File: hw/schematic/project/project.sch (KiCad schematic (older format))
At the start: 10 parts

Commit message: save progress on schematic, experiment on other branch
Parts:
- removed BT?: Battery_Cell, symbol Device:Battery_Cell
- removed U?: MAX1811, Package_SO:SOIC-8_3.9x4.9mm_P1.27mm, symbol Battery_Management:MAX1811
- added C?: 2.2uF, symbol Device:C_Small
- added C?: 0.1uF, symbol Device:C_Small
- added C? (x4): 22uF, symbol Device:C_Small
- added J?: Conn_ARM_JTAG_SWD_10, Connector_PinHeader_1.27mm:PinHeader_2x05_P1.27mm_Vertical_SMD, symbol Connector:Conn_ARM_JTAG_SWD_10
- added U?: MAX32652GWE+, 21-100219C_W1404A4+1, symbol MCU_MAX32652GWE:MAX32652GWE+
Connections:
- net labels added: DM, DP, GND, GPIO, PMU, SDHC_CLK, SDHC_CMD, SDHC_D0, SDHC_D1, SDHC_D2, SDHC_D3, SDHC_WP, SYS, TCK, TDI, TDO, TMS, VBAT, VCC, VIN
- wire segments 0 -> 80
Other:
- note added: "Max input I: 100mA"
- note added: "Max output I: 25mA"
- moved on the sheet: BZ?, J?, M?, SW?, U?, U?B

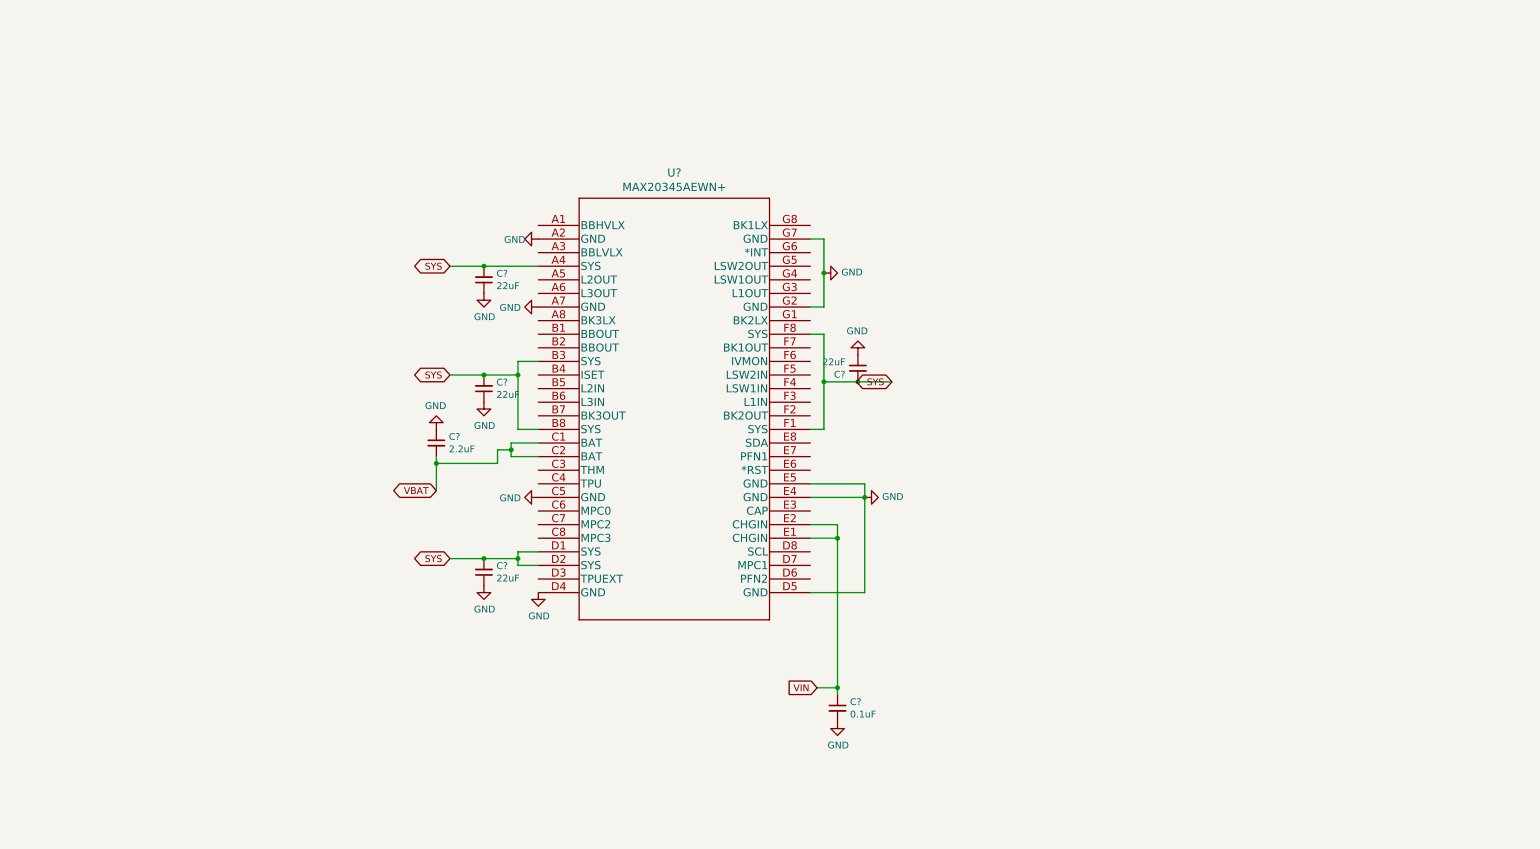
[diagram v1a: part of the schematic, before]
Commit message: end_branch: happy with progress on this branch, will close in favor of reading more of the documentation and getting a firmer understanding of what I must and must not do when drawing a schematic
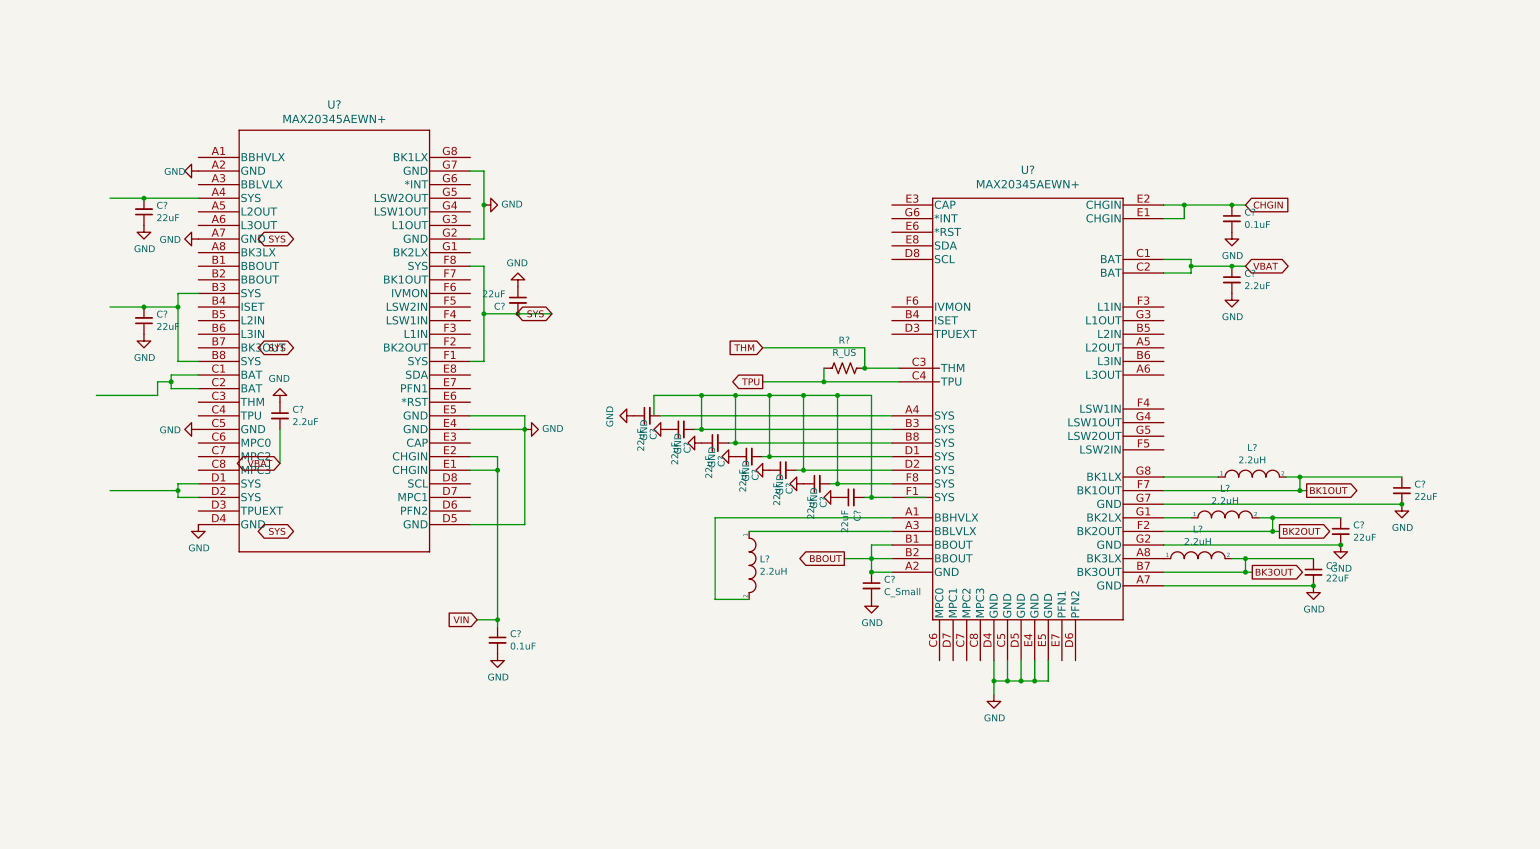
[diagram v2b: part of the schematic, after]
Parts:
- added C? (x9): 22uF, symbol Device:C_Small
- added C?: C_Small, symbol Device:C_Small
- added C?: 2.2uF, symbol Device:C_Small
- added C?: 0.1uF, symbol Device:C_Small
- added L? (x4): 2.2uH, symbol pspice:INDUCTOR
- added R?: R_US, symbol Device:R_US
- added U?: MAX20345AEWN+, 21-100260A_W563H3+1, symbol PMU_MAX20345AEWN_rearranged:MAX20345AEWN+
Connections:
- net labels added: BBOUT, BK1OUT, BK2OUT, BK3OUT, CHGIN, THM, TPU
- wire segments 80 -> 162
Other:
- moved on the sheet: C?, U?
